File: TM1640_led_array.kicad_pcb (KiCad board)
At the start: 2 copper layers, 87.9 x 63 mm, 115 parts, among them J1 TYPE-C-31-M-12, J2 3v3_H, J3 5v_H, Q1 NMOS, Q2 NMOS, Q3 NMOS, Q4 NMOS

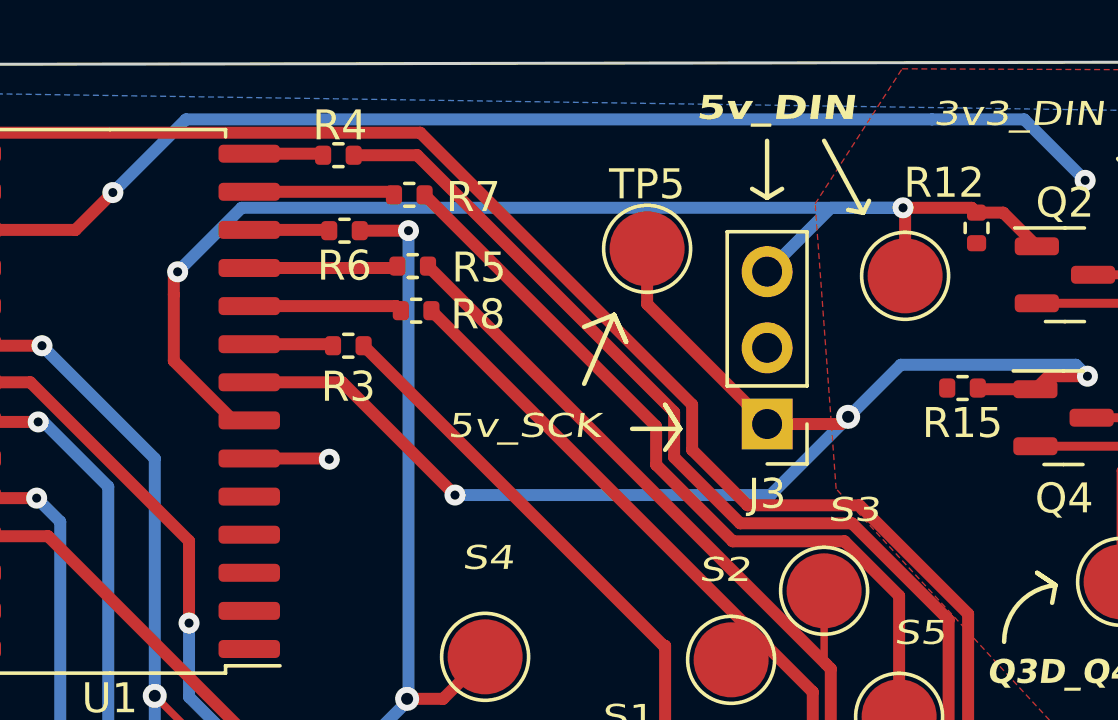
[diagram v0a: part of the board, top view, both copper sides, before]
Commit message: added filter caps to pcb layout
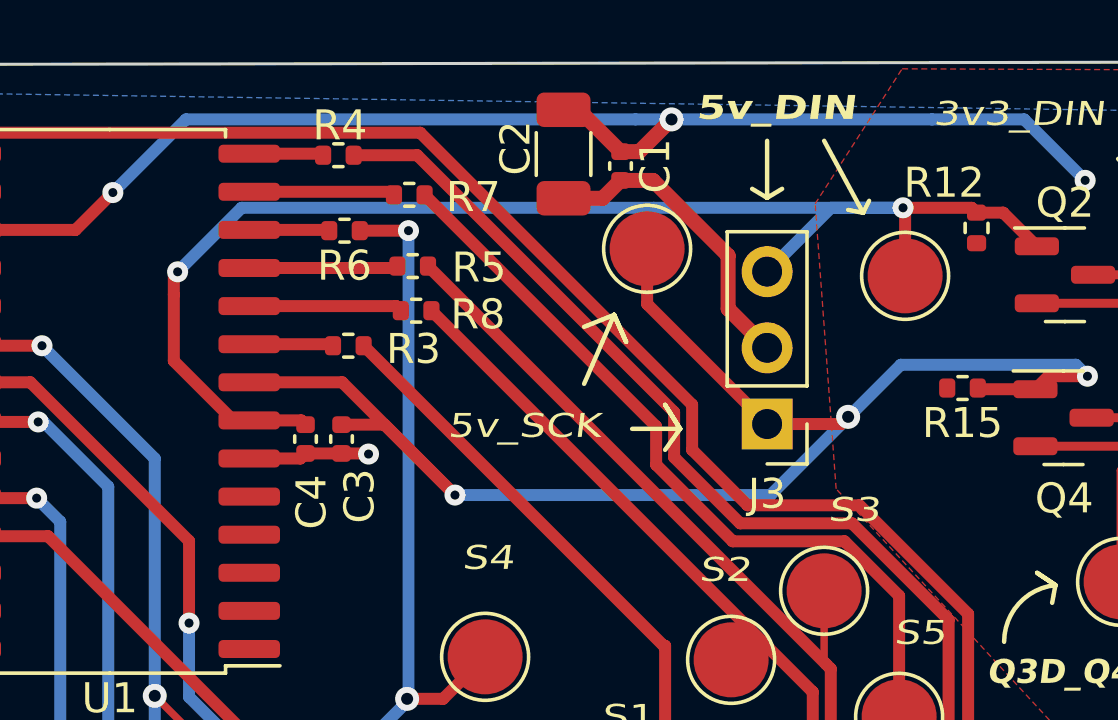
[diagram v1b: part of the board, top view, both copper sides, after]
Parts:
- added C1: 0.1uF, Capacitor_SMD:C_0402_1005Metric, F.Cu at (58.7, 16.9)
- added C2: 100uF, Capacitor_SMD:C_1206_3216Metric, F.Cu at (56.8, 16.5)
- added C3: 100pf, Capacitor_SMD:C_0402_1005Metric, F.Cu at (49.4, 26.0)
- added C4: 100pf, Capacitor_SMD:C_0402_1005Metric, F.Cu at (48.2, 26.0)
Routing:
- net GND: track 20.1 -> 31.8 mm
- net /5V_SCK: track 45.6 -> 50.4 mm
- net VBUS: track 42.2 -> 46.8 mm, vias 2 -> 3
- net /5V_DIN: track 44.1 -> 46.1 mm
